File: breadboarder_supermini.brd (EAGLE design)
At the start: 70.8 x 34.3 mm, 22 parts, among them IC1 AVR-MEGA8-PPTH, Q1 MOSFET-NCHANNEL2N7000

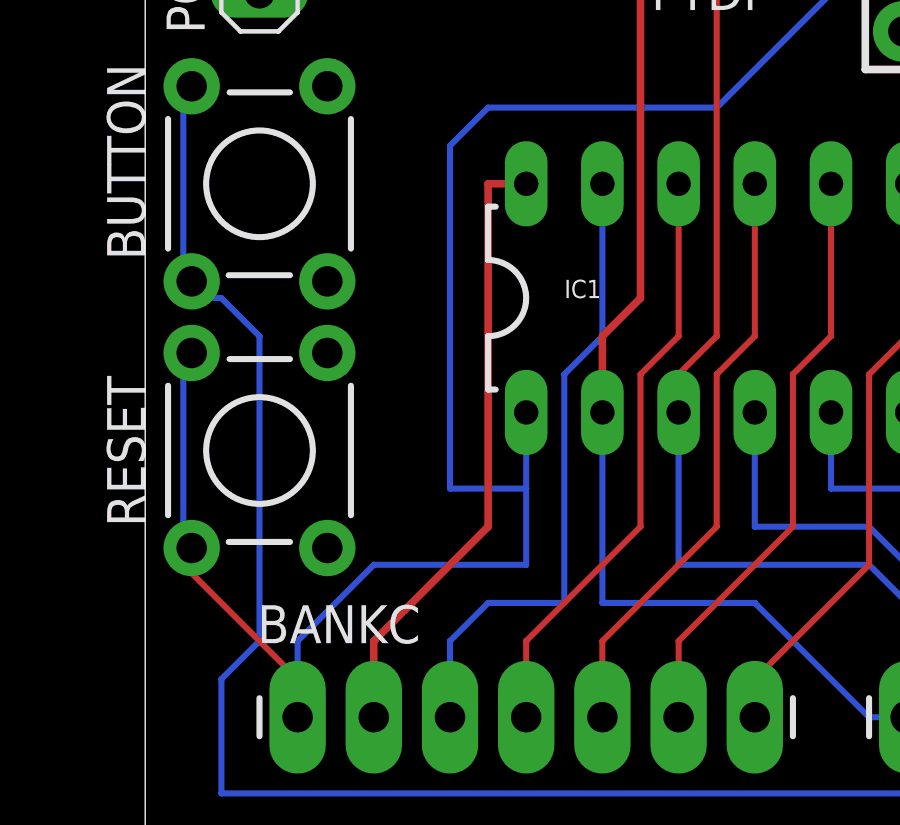
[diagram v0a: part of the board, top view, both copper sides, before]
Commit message: bug with led fet fixed
now can pull to reset line or ground(!), disabling LEDs
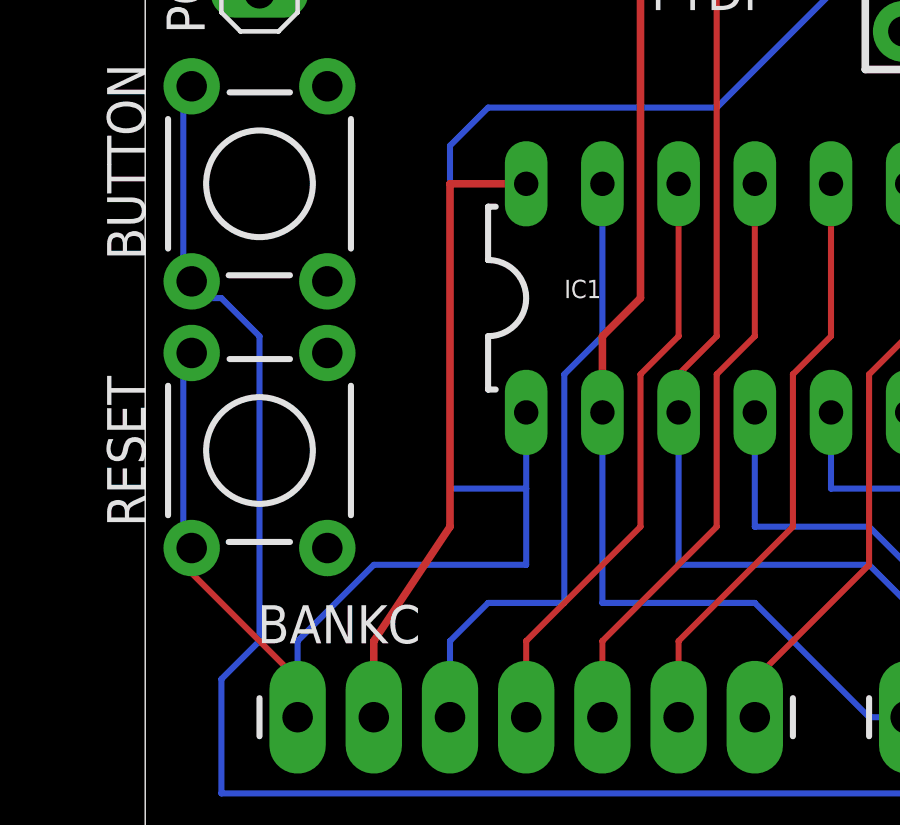
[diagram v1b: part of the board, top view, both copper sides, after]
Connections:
- net GND: now also JP1.1
- net VCC: no longer JP1.1
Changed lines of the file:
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@@
 <wire x1="101.27" y1="33.01" x2="30.48" y2="33.01" width="0" layer="20"/>
 <wire x1="30.48" y1="33.01" x2="30.48" y2="-1.27" width="0" layer="20"/>
-<dimension x1="26.67" y1="36.82" x2="26.67" y2="-1.27" x3="22.86" y3="17.775" textsize="1.778" layer="1"/>
+<dimension x1="26.67" y1="33.01" x2="26.67" y2="-1.27" x3="22.86" y3="15.87" textsize="1.778" layer="1"/>
 <dimension x1="101.27" y1="36.82" x2="30.48" y2="36.82" x3="65.875" y3="38.1" textsize="1.778" layer="1"/>
 </plain>
@@
 <contactref element="BUTTON" pad="4"/>
 <contactref element="BUTTON" pad="3"/>
+<contactref element="JP1" pad="1"/>
 </signal>
 <signal name="VCC">
@@
 <vertex x="101.6" y="43.18"/>
 </polygon>
-<contactref element="JP1" pad="1"/>
 <contactref element="IC1" pad="20"/>
 </signal>
@@
 <contactref element="IC1" pad="28"/>
 <contactref element="BANKC" pad="2"/>
-<wire x1="43.18" y1="20.32" x2="41.91" y2="20.32" width="0.254" layer="1"/>
+<wire x1="43.18" y1="20.32" x2="40.64" y2="20.32" width="0.254" layer="1"/>
 <wire x1="38.1" y1="2.54" x2="38.1" y2="5.08" width="0.254" layer="1"/>
-<wire x1="38.1" y1="5.08" x2="41.91" y2="8.89" width="0.254" layer="1"/>
-<wire x1="41.91" y1="8.89" x2="41.91" y2="20.32" width="0.254" layer="1"/>
+<wire x1="38.1" y1="5.08" x2="40.64" y2="8.89" width="0.254" layer="1"/>
+<wire x1="40.64" y1="8.89" x2="40.64" y2="20.32" width="0.254" layer="1"/>
 </signal>
 <signal name="PB0">

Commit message: tested version minimal classboard
is it a minimal classboard or a mega breadboarder?
8-LED breakout untested, mostly-symmetric design
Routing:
- net GND: track 0.00 -> 89.2 mm
- net PC3: track 19.9 -> 76.1 mm
- net PB4: track 55.7 -> 82.9 mm, vias 2 -> 0
- net PD2: track 73.1 -> 54.2 mm
- net PC1: track 19.9 -> 33.3 mm, vias 0 -> 1
- net PC2: track 19.9 -> 31.1 mm
- net PC4: track 21.4 -> 31.4 mm
- net PB0: track 47.0 -> 40.2 mm, vias 0 -> 1
- net PB7: track 43.3 -> 37.0 mm
- net PB5: track 82.2 -> 86.7 mm
- net PB6: track 46.9 -> 51.2 mm, vias 1 -> 0
- net PB2: track 45.2 -> 42.0 mm, vias 1 -> 0
- net PB1: track 46.6 -> 43.5 mm, vias 2 -> 0
- net PB3: track 50.1 -> 47.3 mm
- net PD3: track 19.6 -> 17.3 mm
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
